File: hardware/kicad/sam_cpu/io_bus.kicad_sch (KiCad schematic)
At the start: 21 parts, among them J9 J9 IO BUS, Q3 2N7002, U6 SN74LVC8T245, U7 74AHCT541

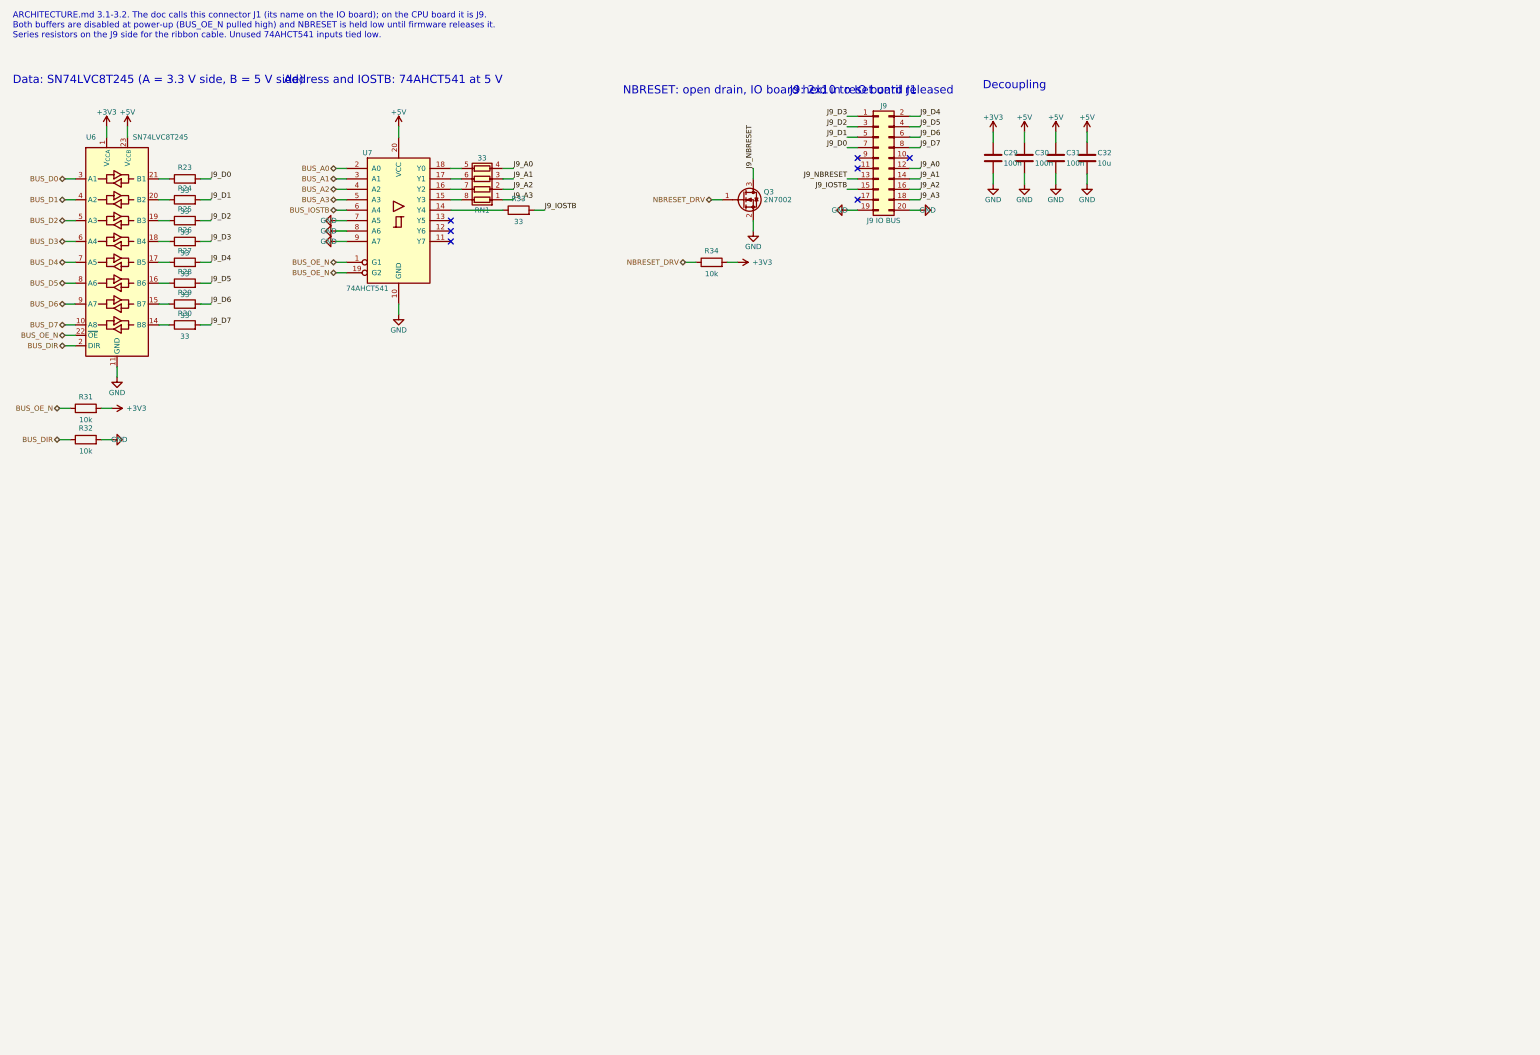
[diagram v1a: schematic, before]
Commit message: Redraw the schematic with wires (draft 0.2)
Every connection is now a wire, and each connector sits on the page of the
parts that drive or read it (Pi header with the RP2354B, J6/J12 with their
comparators and 74HC165, J1 with the 74HC595, J2/J3/J13 with their filters).
Signals between pages use global labels with page references. The Pi page is
merged into the MCU page; the Pi 4 sits on the 40-pin header J21.

ERC: 0 errors, 1 warning. Netlist check: 1266 pins, 299 nets, no differences.

Co-Authored-By: Claude Opus 5.5 (1M context) <noreply@anthropic.com>
Claude-Session: https://claude.ai/code/session_019DLTv1F2PjepjxqiUcAMKV
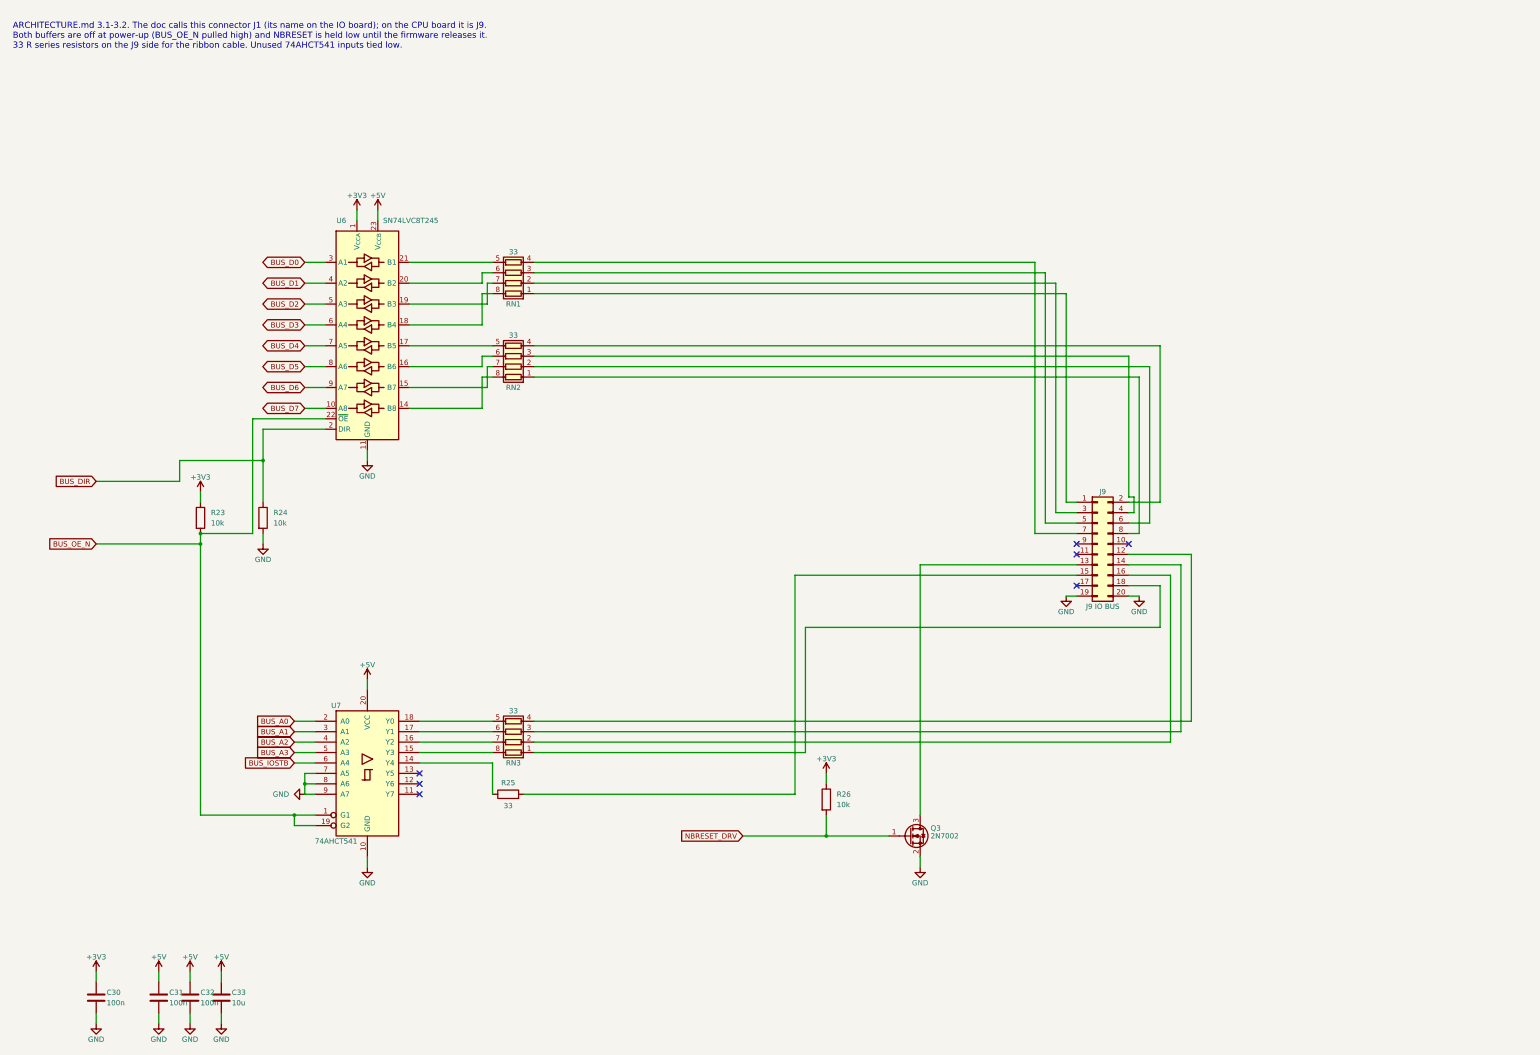
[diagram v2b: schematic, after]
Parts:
- removed C29: 100n, Capacitor_SMD:C_0603_1608Metric, symbol Device:C
- removed R27, R28, R29, R30, R33: 33, Resistor_SMD:R_0603_1608Metric, symbol Device:R
- removed R31, R32, R34: 10k, Resistor_SMD:R_0603_1608Metric, symbol Device:R
- added C33: 10u, Capacitor_SMD:C_0805_2012Metric, symbol Device:C
- added RN2, RN3: 33, Resistor_SMD:R_Array_Convex_4x0603, symbol Device:R_Pack04
- C32: value 10u -> 100n; footprint Capacitor_SMD:C_0805_2012Metric -> Capacitor_SMD:C_0603_1608Metric
- R23, R24, R26: value 33 -> 10k
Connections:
- net J9_IOSTB is gone; now on an unnamed net: J9.15 (Pin_15)
- net +3V3: now also C30.1, R23.1, R26.1
- net +5V: now also C33.1; no longer C30.1
- net BUS_DIR: now also R24.1
- net BUS_OE_N: now also R23.2
- net GND: now also R24.2, C33.2
- net NBRESET_DRV: now also R26.2
- net at U6.15 (B7): now also RN2.7 (R2.2)
- net at U7.14 (Y4): now also R25.1
- net at U6.14 (B8): now also RN2.8 (R1.2)
- net at U6.16 (B6): now also RN2.6 (R3.2)
- net at U6.17 (B5): now also RN2.5 (R4.2)
- net at U6.18 (B4): now also RN1.8 (R1.2); no longer R26.1
- net at U6.19 (B3): now also RN1.7 (R2.2); no longer R25.1
- net at U6.20 (B2): now also RN1.6 (R3.2); no longer R24.1
- net at U6.21 (B1): now also RN1.5 (R4.2); no longer R23.1
- net at U7.15 (Y3): now also RN3.8 (R1.2); no longer RN1.8 (R1.2)
- net at U7.16 (Y2): now also RN3.7 (R2.2); no longer RN1.7 (R2.2)
- net at U7.17 (Y1): now also RN3.6 (R3.2); no longer RN1.6 (R3.2)
- net at U7.18 (Y0): now also RN3.5 (R4.2); no longer RN1.5 (R4.2)
- net J9_A0: no longer names the net of J9.12 (Pin_12)
- net J9_A0: now also RN3.4 (R4.1); no longer RN1.4 (R4.1)
- net J9_A1: no longer names the net of J9.14 (Pin_14)
- net J9_A1: now also RN3.3 (R3.1); no longer RN1.3 (R3.1)
- net J9_A2: no longer names the net of J9.16 (Pin_16)
- net J9_A2: now also RN3.2 (R2.1); no longer RN1.2 (R2.1)
- net J9_A3: no longer names the net of RN1.1 (R1.1)
- net J9_A3: now also J9.1 (Pin_1); no longer J9.18 (Pin_18)
- net J9_D0: no longer names the net of J9.7 (Pin_7)
- net J9_D0: now also RN1.4 (R4.1); no longer R23.2
- net J9_D1: no longer names the net of J9.5 (Pin_5)
- net J9_D1: now also RN1.3 (R3.1); no longer R24.2
- net J9_D2: no longer names the net of R25.2
- net J9_D2: no longer J9.3 (Pin_3)
- removed net J9_D3: J9.1 (Pin_1), R26.2
- net J9_D4: no longer names the net of J9.2 (Pin_2)
- net J9_D4: now also RN2.4 (R4.1)
- net J9_D5: no longer names the net of J9.4 (Pin_4)
- net J9_D5: now also RN2.3 (R3.1)
- net J9_D6: no longer names the net of J9.6 (Pin_6)
- net J9_D6: now also RN2.2 (R2.1)
- net J9_D7: no longer names the net of J9.8 (Pin_8)
- net J9_D7: now also RN2.1 (R1.1)
- net J9_NBRESET: no longer names the net of J9.13 (Pin_13), Q3.3 (D)
- new net: J9.18 (Pin_18), RN3.1 (R1.1)
- new net: J9.3 (Pin_3), RN1.2 (R2.1)
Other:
- note added: "ARCHITECTURE.md 3.1-3.2. The doc calls this connector J1 (its name on the IO board); on the CPU board it is J9. Both buffers are off at power-up (BUS_OE_N pulled high) and NBRESET is held low until the firmware releases it. 33 R series resistors on the J9 side for the ribbon cable. Unused 74AHCT541 inputs tied low."
- note removed: "ARCHITECTURE.md 3.1-3.2. The doc calls this connector J1 (its name on the IO board); on the CPU board it is J9. Both buffers are disabled at power-up (BUS_OE_N pulled high) and NBRESET is held low until firmware releases it. Series resistors on the J9 side for the ribbon cable. Unused 74AHCT541 inputs tied low."
- note removed: "Address and IOSTB: 74AHCT541 at 5 V"
- note removed: "Data: SN74LVC8T245 (A = 3.3 V side, B = 5 V side)"
- note removed: "Decoupling"
- note removed: "J9: 2x10 to IO board J1"
- note removed: "NBRESET: open drain, IO board held in reset until released"
- moved on the sheet: C30, C31, C32, J9, Q3, R23, R24, R25, R26, RN1, U6, U7

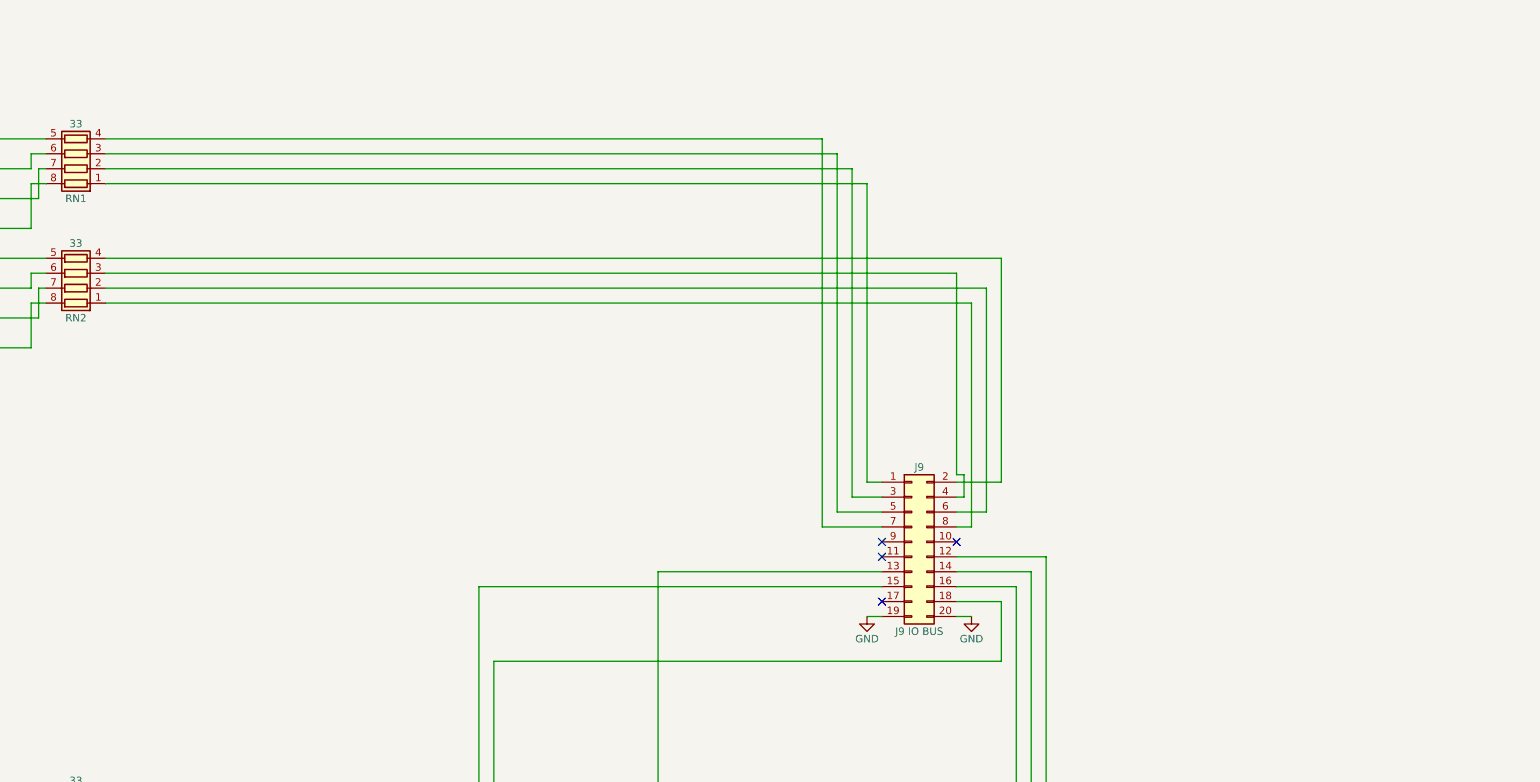
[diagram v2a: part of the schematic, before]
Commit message: Add RTC, test points and stereo speaker connector; place all parts on 2 layers
Schematic: DS3231MZ real-time clock on the Pi I2C1 with a CR2032 holder,
22 test points (rails, bus, strobes, switch chain, VREF, DAC outputs) and
J22, a second KK-396 speaker connector with L and R as separate pairs.
ERC 0 errors, generated netlist matches the intended nets.

PCB: 2 copper layers. The RP2354B sits near J9 with its USB-C on the top
edge 13 mm from the USB pins; decoupling, regulator and crystal parts on
their pins; every other part grouped by sheet next to its connector, low
parts only under the Pi. J17 and J22 on the right edge; Pi and J5 12 mm
lower to fit the audio parts.

Co-Authored-By: Claude Opus 5.5 (1M context) <noreply@anthropic.com>
Claude-Session: https://claude.ai/code/session_01ExuDVoDDDHhVWjb8EwVzYb
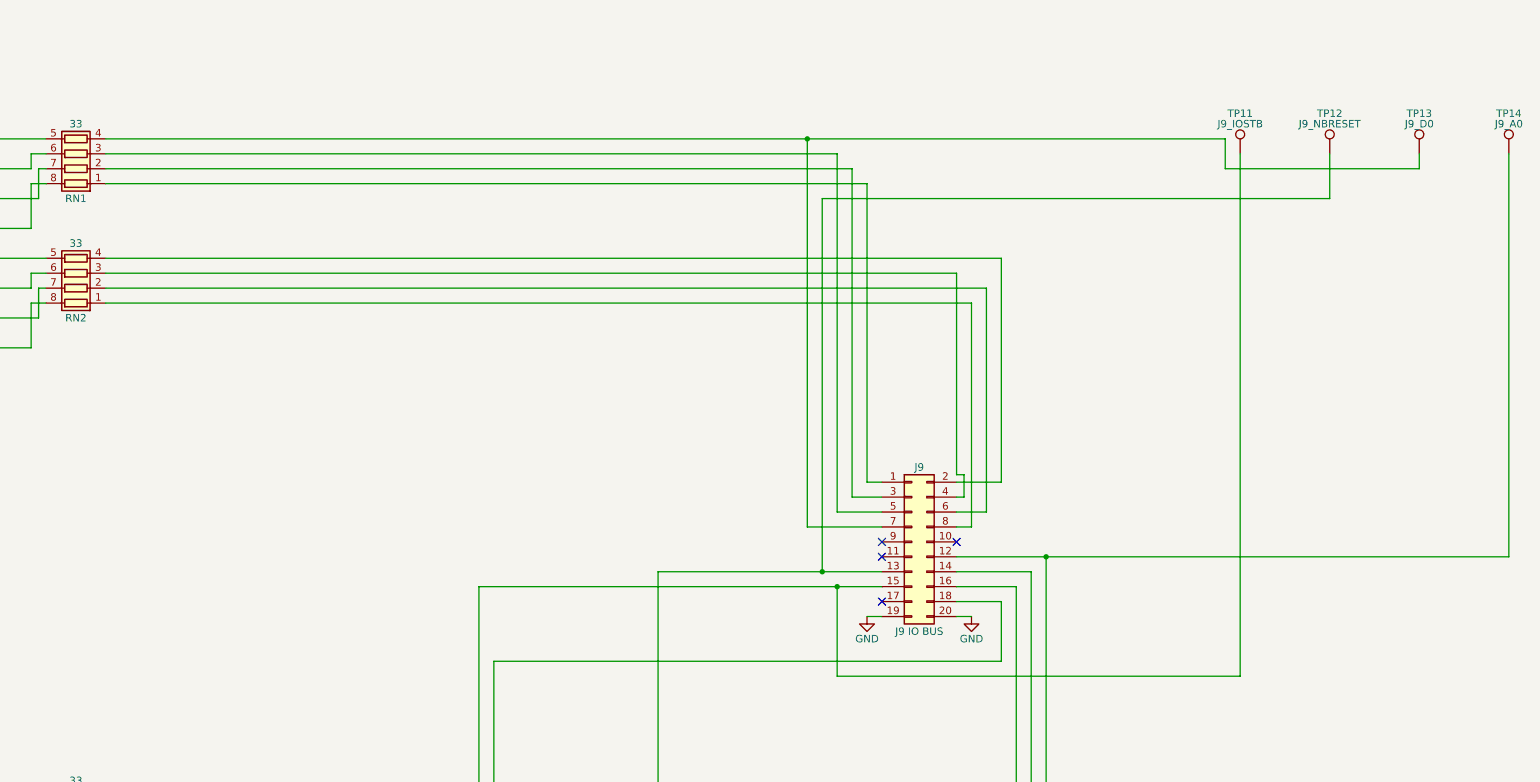
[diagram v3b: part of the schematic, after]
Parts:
- added TP11: J9_IOSTB, TestPoint:TestPoint_Pad_D1.5mm, symbol Connector:TestPoint
- added TP12: J9_NBRESET, TestPoint:TestPoint_Pad_D1.5mm, symbol Connector:TestPoint
- added TP13: J9_D0, TestPoint:TestPoint_Pad_D1.5mm, symbol Connector:TestPoint
- added TP14: J9_A0, TestPoint:TestPoint_Pad_D1.5mm, symbol Connector:TestPoint
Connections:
- net at J9.15 (Pin_15), R25.2: now also TP11.1
- net at J9.13 (Pin_13), Q3.3 (D): now also TP12.1
- net at J9.12 (Pin_12), RN3.4 (R4.1): now also TP14.1
- net at J9.7 (Pin_7), RN1.4 (R4.1): now also TP13.1

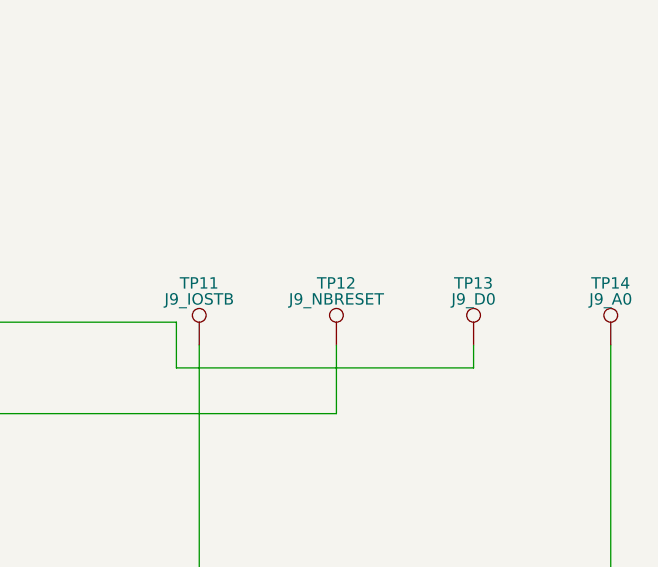
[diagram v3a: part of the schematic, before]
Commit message: Audio on external 12 V with TDA7297 stereo + subwoofer amps, NCP1117, guide regulator layout
- Remove the +-12 V input from J11; J23 external +12 V with polyfuse and TVS
- Replace the two TDA2030A with a TDA7297 bridge amp for left/right (J10, J22)
  and a second TDA7297 for the subwoofer (J24), fed by an (L+R)/2 110 Hz
  Sallen-Key low-pass (OPA1678); shared standby and RP2354B-controlled mute
- AMS1117 -> NCP1117-3.3 (ceramic-stable, as in the RP2350 guide), 10 uF 1206
- L1 and crystal part numbers from the RP2350 hardware guide
- Place the core regulator parts by hand following the Pico 2 layout; amps in a
  row with a heatsink keep-out; J23/J22/J24 on the right edge

Co-Authored-By: Claude Opus 5.5 (1M context) <noreply@anthropic.com>
Claude-Session: https://claude.ai/code/session_01ExuDVoDDDHhVWjb8EwVzYb
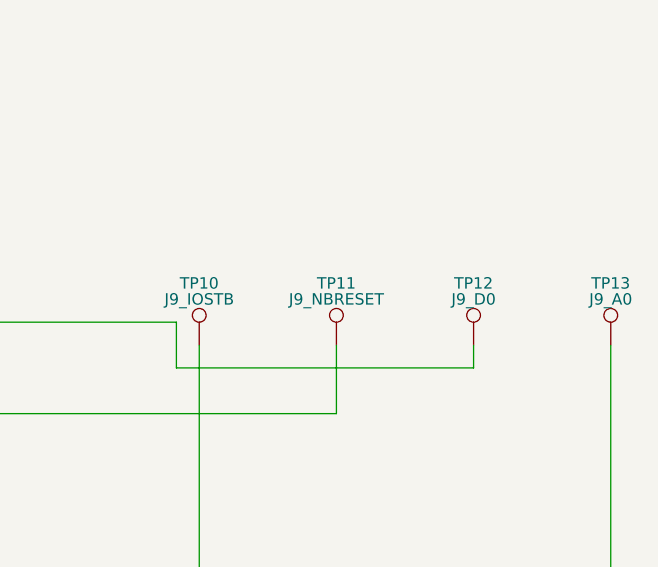
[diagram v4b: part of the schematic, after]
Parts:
- removed TP14: J9_A0, TestPoint:TestPoint_Pad_D1.5mm, symbol Connector:TestPoint
- added TP10: J9_IOSTB, TestPoint:TestPoint_Pad_D1.5mm, symbol Connector:TestPoint
- TP11: value J9_IOSTB -> J9_NBRESET
- TP12: value J9_NBRESET -> J9_D0
- TP13: value J9_D0 -> J9_A0
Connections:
- net at J9.12 (Pin_12), RN3.4 (R4.1): now also TP13.1
- net at J9.15 (Pin_15), R25.2: now also TP10.1; no longer TP11.1
- net at J9.7 (Pin_7), RN1.4 (R4.1): now also TP12.1; no longer TP13.1
- net at J9.13 (Pin_13), Q3.3 (D): now also TP11.1; no longer TP12.1
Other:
- moved on the sheet: TP11, TP12, TP13
